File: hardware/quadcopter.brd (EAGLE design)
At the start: 126.2 x 126.2 mm, 85 parts, among them J1 AVR_SPI_PRG_6NS, J2 HEADER-4POS-0.1IN-FEMALE-SMD-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, J3 HEADER-10POSTH-254X10, J4 HEADER-4POS-0.1IN-FEMALE-SMD-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, M1 MOTOR_PADS_GND-MOLEX-SMD, M2 MOTOR_PADS_GND-MOLEX-SMD, M3 MOTOR_PADS_GND-MOLEX-SMD, M4 MOTOR_PADS_GND-MOLEX-SMD, Q1 MOSFET-SI2302CDS-T1-E3CT-ND, Q2 MOSFET-SI2302CDS-T1-E3CT-ND, Q3 MOSFET-SI2302CDS-T1-E3CT-ND, Q4 MOSFET-SI2302CDS-T1-E3CT-ND, Q5 MOSFET-SI2302CDS-T1-E3CT-ND, Q6 MOSFET-SI2302CDS-T1-E3CT-ND, Q7 MOSFET-SI2302CDS-T1-E3CT-ND, Q8 MOSFET-SI2302CDS-T1-E3CT-ND, Q9 MOSFET-SI2302CDS-T1-E3CT-ND, SW1 PUSHBUTTON_SMD-VERTICAL-1, U1 ATMEGA128RFA1, U2 LSM-IMU-497-18367-1-NDIMU, Y1 CRYSTAL5X3

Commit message: fixed quick check
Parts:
- moved R7 0.12 mm to (-3.00, -9.00)
- moved J4 0.05 mm to (-12.0, -14.0)
- renumbered NET_BRIDGE to NB, REG to RG
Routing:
- net VBAT: track 129.4 -> 93.1 mm, vias 19 -> 25
- net BAT_GND: track 85.3 -> 70.3 mm, vias 24 -> 26
- net GND: track 741.5 -> 737.6 mm
- net MISO: track 29.3 -> 30.3 mm
- net 3V: track 135.0 -> 134.0 mm
- net RED: track 395.8 -> 395.2 mm
- net BLU: track 234.4 -> 233.9 mm
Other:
- board text removed: "2 mm"
- board text removed: "height: 126.2 mm"

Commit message: fixed quickcheck part 2
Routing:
- net VBAT: track 93.1 -> 86.5 mm
- net GND: track 737.6 -> 741.4 mm
- net RED: track 395.2 -> 394.6 mm

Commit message: changed part names
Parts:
- renumbered NB to NB1, RG to RG1
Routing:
- net VBAT: vias 25 -> 24
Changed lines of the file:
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@@
 <attribute name="NAME" x="-17" y="24" size="0.9" layer="25" font="vector" align="center"/>
 </element>
-<element name="NB" library="custom_" library_urn="urn:adsk.wipprod:fs.file:vf.FjMADskDQ2Se9fX1PD5xcw" package="NET_BRIDGE" value="NET-BRIDGE" x="-2" y="-22.5" smashed="yes">
+<element name="NB1" library="custom_" library_urn="urn:adsk.wipprod:fs.file:vf.FjMADskDQ2Se9fX1PD5xcw" package="NET_BRIDGE" value="NET-BRIDGE" x="-2" y="-22.5" smashed="yes">
 <attribute name="CREATOR" value="ELAINE" x="27.21" y="-84.73" size="1.778" layer="27" display="off"/>
 <attribute name="DIST" value="NA" x="27.21" y="-84.73" size="1.778" layer="27" display="off"/>
@@
 <attribute name="VALUE" x="-22" y="6.5" size="0.9" layer="27" font="vector" align="center"/>
 </element>
-<element name="RG" library="quadparts_prebuilt_2022" package="SOT23-DBV" value="3V" x="-3" y="-16.5" smashed="yes">
+<element name="RG1" library="quadparts_prebuilt_2022" package="SOT23-DBV" value="3V" x="-3" y="-16.5" smashed="yes">
 <attribute name="CREATOR" value="Swanson" x="24.94" y="-46.98" size="1.778" layer="27" display="off"/>
 <attribute name="DATASHEET" value="http://www.ti.com/lit/ds/symlink/lp3985.pdf" x="24.94" y="-46.98" size="1.778" layer="27" display="off"/>
@@
 <contactref element="R22" pad="2"/>
 <contactref element="R21" pad="2"/>
-<contactref element="RG" pad="2"/>
+<contactref element="RG1" pad="2"/>
 <contactref element="C13" pad="2"/>
-<contactref element="NB" pad="2"/>
+<contactref element="NB1" pad="2"/>
 <contactref element="J4" pad="3"/>
 <contactref element="J3" pad="1"/>
@@
 <contactref element="R18" pad="1"/>
 <contactref element="R19" pad="1"/>
-<contactref element="RG" pad="5"/>
+<contactref element="RG1" pad="5"/>
 <contactref element="C13" pad="1"/>
 <contactref element="C17" pad="1"/>
@@
 <contactref element="D5" pad="1"/>
 <contactref element="S1" pad="B"/>
-<contactref element="RG" pad="1"/>
+<contactref element="RG1" pad="1"/>
 <contactref element="C15" pad="1"/>
 <contactref element="B2" pad="2"/>
@@
 <wire x1="30.870865625" y1="2.158478125" x2="30.5" y2="2.2346" width="0.762" layer="16"/>
 <wire x1="-3.95" y1="-17.8" x2="-3.9116" y2="-19.2637" width="0.762" layer="1"/>
-<via x="-4" y="-3.5" extent="1-16" drill="0.6096">
-</via>
 <via x="-18" y="5" extent="1-16" drill="0.6096">
 </via>
@@
 <contactref element="S1" pad="A"/>
 <contactref element="B2" pad="1"/>
-<contactref element="NB" pad="1"/>
+<contactref element="NB1" pad="1"/>
 <contactref element="J3" pad="4"/>
 <contactref element="R1" pad="1"/>
@@
 </signal>
 <signal name="N$20">
-<contactref element="RG" pad="3"/>
+<contactref element="RG1" pad="3"/>
 <contactref element="S1" pad="C"/>
 <wire x1="-1.1176" y1="-30.24505" x2="-2.30505" y2="-29.0576" width="0.127" layer="1"/>

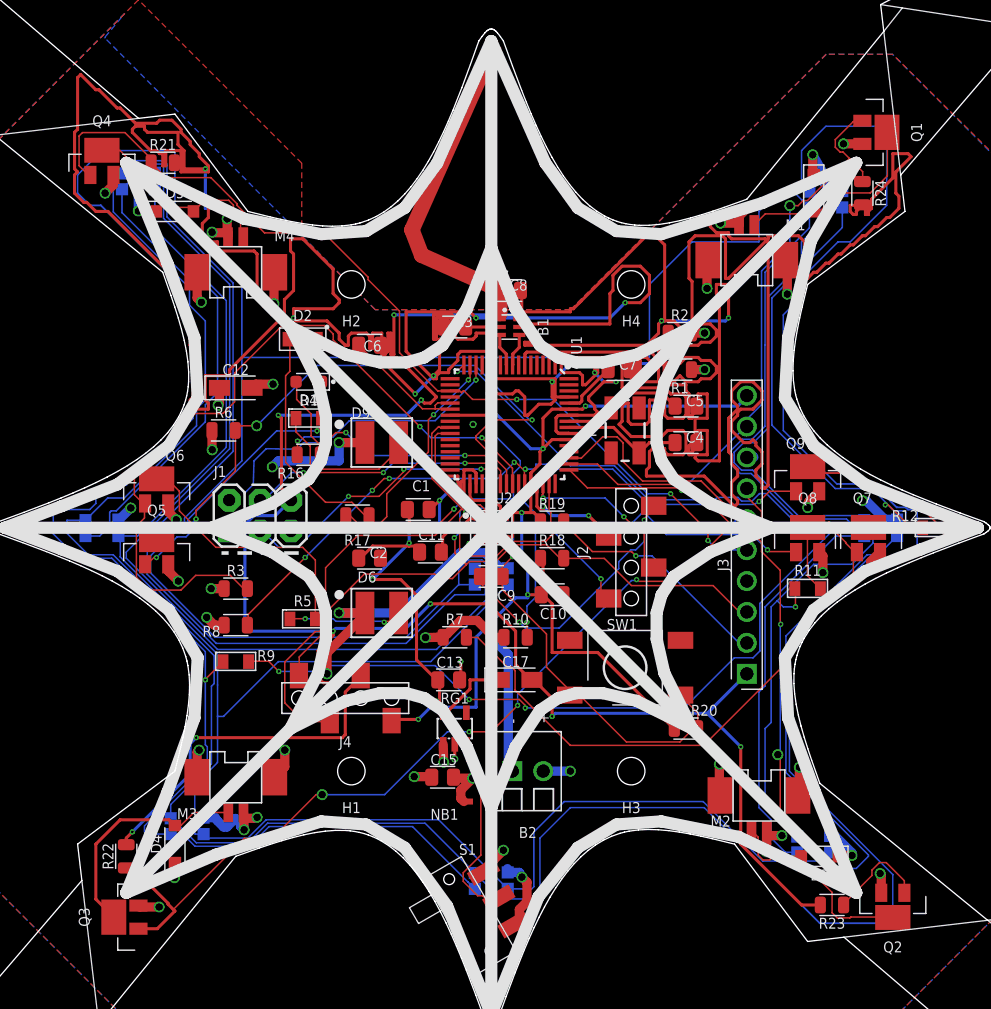
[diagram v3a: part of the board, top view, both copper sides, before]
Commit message: fixed full check issues
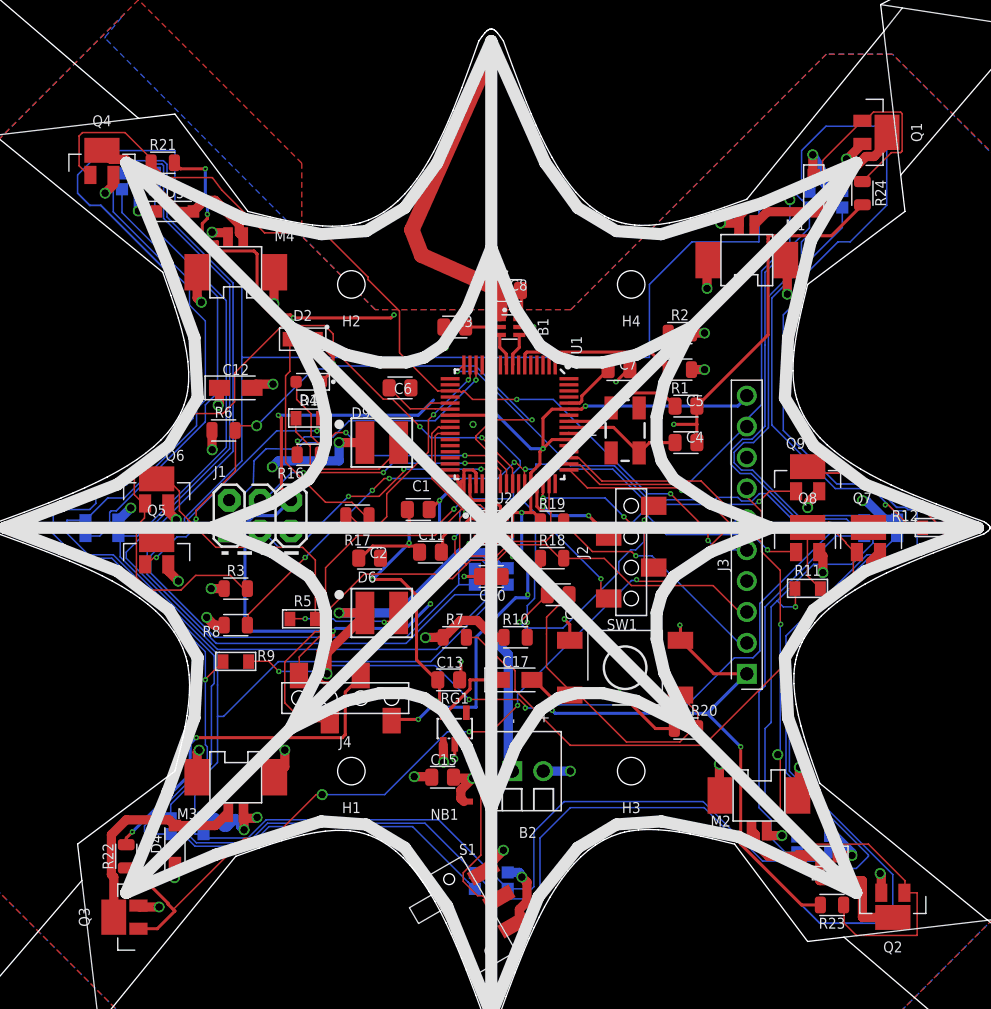
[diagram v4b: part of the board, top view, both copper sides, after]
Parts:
- moved C9 5.70 mm to (5.50, -5.50)
- moved C10 5.22 mm to (0.00, -4.00)
- moved C6 4.30 mm to (-7.50, 11.5)
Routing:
- net GND: track 741.4 -> 246.3 mm, vias 34 -> 31
- net 3V: track 134.0 -> 120.1 mm, vias 11 -> 14
- net PWM2: track 63.6 -> 72.4 mm
- net PWM1: track 51.1 -> 58.3 mm
- net VBAT: track 86.5 -> 83.0 mm, vias 24 -> 22
- net N$9: track 11.3 -> 8.05 mm
- net PWM3: track 89.2 -> 86.9 mm
- net RESET: track 66.7 -> 68.4 mm
- net N$11: track 22.1 -> 20.4 mm
- net N$14: track 16.2 -> 14.8 mm
- net N$16: track 19.0 -> 17.6 mm
- net BAT_GND: track 70.3 -> 69.1 mm
- net N$15: track 17.0 -> 17.9 mm
- net N$17: track 16.4 -> 15.7 mm

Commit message: finished fixing review
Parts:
- J1: value AVR_SPI_PRG_6NS -> AVR_SPI_PRG_6-SMD; device quadparts_prebuilt_2022:2X3-NS -> quadparts_prebuilt_2022:2X3-SMD
- moved R12 57.7 mm to (-21.0, -4.50), flipped to the bottom
- moved Q9 47.2 mm to (-21.0, -0.50), flipped to the bottom
- moved J1 47.2 mm to (28.2, -0.01), turned to 90 degrees
- moved R9 38.6 mm to (16.0, 0.00), flipped to the bottom
- moved Q8 34.7 mm to (0.00, -24.0), flipped to the bottom
- moved R11 27.6 mm to (6.00, -24.0), flipped to the bottom
- moved D1 26.6 mm to (-13.0, -14.5)
- moved R17 21.5 mm to (-32.5, 1.50)
- moved R16 19.0 mm to (-32.5, -1.50)
- moved R7 19.0 mm to (16.0, -10.0), flipped to the bottom
- moved R22 17.7 mm to (-17.0, -15.0)
- moved C9 17.6 mm to (-11.0, -11.5)
- moved R10 15.7 mm to (-5.00, -23.0), flipped to the bottom
- moved Q3 14.9 mm to (-20.0, -21.0)
- moved Q7 14.4 mm to (17.1, -4.50), flipped to the bottom
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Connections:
- net 3V: now also J1.2
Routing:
- net GND: track 246.3 -> 66.8 mm, vias 31 -> 25
- net SCK: track 23.3 -> 73.8 mm, vias 3 -> 8
- net MISO: track 30.3 -> 78.4 mm, vias 3 -> 10
- net N$1: track 6.86 -> 49.9 mm, vias 0 -> 4
- net PG2: track 86.4 -> 44.3 mm, vias 2 -> 7
- net PG0: track 19.1 -> 61.2 mm, vias 2 -> 5
- net RESET: track 68.4 -> 109.6 mm, vias 3 -> 7
- net N$2: track 19.0 -> 54.8 mm, vias 0 -> 4
- net PG1: track 19.5 -> 51.2 mm, vias 2 -> 6
- net MOSI: track 21.9 -> 47.1 mm, vias 3 -> 6
- net SCL: track 75.4 -> 51.6 mm
- net PB7: track 55.0 -> 34.4 mm, vias 6 -> 2
- net RED: track 394.6 -> 375.4 mm
- net PWM2: track 72.4 -> 53.9 mm
- net N$11: track 20.4 -> 37.8 mm, vias 2 -> 4
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
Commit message: fixed quick check
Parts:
- moved J1 0.19 mm to (28.0, 0.00)
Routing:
- net BAT_GND: track 62.9 -> 61.2 mm
- net 3V: track 123.8 -> 125.0 mm

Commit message: fixed quick check 2
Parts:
- moved Q7 0.07 mm to (17.0, -4.50)
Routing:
- net SCL: track 51.6 -> 52.5 mm
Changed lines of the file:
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@@
 <attribute name="VALUE" x="-29.5" y="-2.5" size="0.9" layer="28" font="vector" rot="MR0"/>
 </element>
-<element name="Q7" library="custom_" library_urn="urn:adsk.wipprod:fs.file:vf.FjMADskDQ2Se9fX1PD5xcw" package="SOT95P240X110-3MOSFET" value="MOSFET-SI2302CDS-T1-E3CT-ND" x="17.0726" y="-4.5" smashed="yes" rot="MR0">
-<attribute name="CREATOR" value="ELENA" x="23.0726" y="3.5" size="1.778" layer="28" rot="MR0" display="off"/>
-<attribute name="DIST" value="Digikey" x="23.0726" y="3.5" size="1.778" layer="28" rot="MR0" display="off"/>
-<attribute name="DISTPN" value="SI2302CDS-T1-E3CT-ND" x="23.0726" y="3.5" size="1.778" layer="28" rot="MR0" display="off"/>
-<attribute name="NAME" x="17.5726" y="-1.5" size="0.9" layer="26" font="vector" rot="MR0" align="bottom-center"/>
+<element name="Q7" library="custom_" library_urn="urn:adsk.wipprod:fs.file:vf.FjMADskDQ2Se9fX1PD5xcw" package="SOT95P240X110-3MOSFET" value="MOSFET-SI2302CDS-T1-E3CT-ND" x="17" y="-4.5" smashed="yes" rot="MR0">
+<attribute name="CREATOR" value="ELENA" x="23" y="3.5" size="1.778" layer="28" rot="MR0" display="off"/>
+<attribute name="DIST" value="Digikey" x="23" y="3.5" size="1.778" layer="28" rot="MR0" display="off"/>
+<attribute name="DISTPN" value="SI2302CDS-T1-E3CT-ND" x="23" y="3.5" size="1.778" layer="28" rot="MR0" display="off"/>
+<attribute name="NAME" x="17.5" y="-1.5" size="0.9" layer="26" font="vector" rot="MR0" align="bottom-center"/>
 </element>
 <element name="R7" library="quadparts_prebuilt_2022" package="RESC2012X60_HS" value="10K" x="16" y="-10" smashed="yes" rot="MR0">
@@
 <wire x1="21.5" y1="23.05" x2="20.26176875" y2="21.81176875" width="0.762" layer="1"/>
 <wire x1="20.26176875" y1="21.81176875" x2="20.18623125" y2="21.81176875" width="0.762" layer="1"/>
-<wire x1="16.955" y1="-10" x2="18.2546" y2="-10" width="0.762" layer="16"/>
 <wire x1="-20.045" y1="3.5" x2="-18.7454" y2="3.5" width="0.762" layer="16"/>
 <wire x1="-21.95" y1="-1.5" x2="-21.95" y2="-2.8596" width="0.762" layer="16"/>
-<via x="18.2546" y="-10" extent="1-16" drill="0.6096">
-</via>
 <via x="-18.7454" y="3.5" extent="1-16" drill="0.6096">
 </via>
@@
 <wire x1="-2.5" y1="-24" x2="-2.20434375" y2="-24" width="0.762" layer="16"/>
 <wire x1="-2.20434375" y1="-24" x2="-1.67094375" y2="-24.5334" width="0.762" layer="16"/>
-<via x="18" y="-7" extent="1-16" drill="0.762">
-</via>
-<wire x1="16.1226" y1="-5.5" x2="16.9892" y2="-6.3666" width="0.762" layer="16"/>
-<wire x1="16.9892" y1="-6.3666" x2="16.9892" y2="-6.47094375" width="0.762" layer="16"/>
-<wire x1="16.9892" y1="-6.47094375" x2="17.51825625" y2="-7" width="0.762" layer="16"/>
-<wire x1="17.51825625" y1="-7" x2="18" y2="-7" width="0.762" layer="16"/>
+<via x="17.75" y="-6.9739" extent="1-16" drill="0.762">
+</via>
 <via x="-17.67299375" y="-21.16489375" extent="1-16" drill="0.6096">
 </via>
@@
 <wire x1="-22.9166" y1="20.52905625" x2="-22.9166" y2="20.6334" width="0.762" layer="1"/>
 <wire x1="-22.9166" y1="20.6334" x2="-22.05" y2="21.5" width="0.762" layer="1"/>
+<via x="18.23839375" y="-10.01620625" extent="1-16" drill="0.6096">
+</via>
+<wire x1="16.955" y1="-10" x2="18.2221875" y2="-10" width="0.762" layer="16"/>
+<wire x1="18.2221875" y1="-10" x2="18.23839375" y2="-10.01620625" width="0.762" layer="16"/>
+<wire x1="16.05" y1="-5.5" x2="16.9166" y2="-6.3666" width="0.762" layer="16"/>
+<wire x1="16.9166" y1="-6.3666" x2="16.9166" y2="-6.47094375" width="0.762" layer="16"/>
+<wire x1="16.9166" y1="-6.47094375" x2="17.41955625" y2="-6.9739" width="0.762" layer="16"/>
+<wire x1="17.41955625" y1="-6.9739" x2="17.75" y2="-6.9739" width="0.762" layer="16"/>
 </signal>
 <signal name="PWM2">
@@
 <wire x1="10.5444125" y1="-13.0444125" x2="8.990175" y2="-14.59865" width="0.127" layer="16"/>
 <wire x1="8.990175" y1="-14.59865" x2="2.16535" y2="-14.59865" width="0.127" layer="16"/>
-<wire x1="16.028825" y1="-7.56" x2="12.729675" y2="-4.26085" width="0.127" layer="16"/>
-<wire x1="11.94435" y1="-4.26085" x2="12.729675" y2="-4.26085" width="0.127" layer="16"/>
-<wire x1="16.028825" y1="-7.56" x2="16.028825" y2="-8.971175" width="0.127" layer="16"/>
 <wire x1="16.028825" y1="-8.971175" x2="16" y2="-9" width="0.127" layer="16"/>
 <wire x1="16" y1="-9" x2="15.9555875" y2="-9.0444125" width="0.127" layer="16"/>
@@
 <wire x1="14.5" y1="-13" x2="14.4555875" y2="-13.0444125" width="0.127" layer="16"/>
 <wire x1="14.4555875" y1="-13.0444125" x2="10.5444125" y2="-13.0444125" width="0.127" layer="16"/>
+<wire x1="11.94435" y1="-4.26085" x2="13.6273" y2="-5.9438" width="0.127" layer="16"/>
+<wire x1="13.6273" y1="-5.9438" x2="13.6273" y2="-6.45516875" width="0.127" layer="16"/>
+<wire x1="16.028825" y1="-8.85669375" x2="16.028825" y2="-8.971175" width="0.127" layer="16"/>
+<wire x1="13.6273" y1="-6.45516875" x2="16.028825" y2="-8.85669375" width="0.127" layer="16"/>
 </signal>
 <signal name="PWM4">
@@
 <wire x1="-2.0955" y1="1.2573" x2="-2.4445" y2="0.9083" width="0.127" layer="1"/>
 <wire x1="-2.4445" y1="0.9083" x2="-2.4445" y2="-1.31291875" width="0.127" layer="1"/>
-<wire x1="11.8745" y1="-2.30505" x2="15.4067" y2="-5.83725" width="0.127" layer="16"/>
-<wire x1="15.4067" y1="-5.83725" x2="15.4067" y2="-6.33943125" width="0.127" layer="16"/>
-<wire x1="19.10385625" y1="-9.42975" x2="20.955" y2="-9.42975" width="0.127" layer="16"/>
+<wire x1="11.8745" y1="-2.30505" x2="13.9067" y2="-4.33725" width="0.127" layer="16"/>
+<wire x1="13.9067" y1="-4.33725" x2="13.9067" y2="-6.33943125" width="0.127" layer="16"/>
+<wire x1="18.60385625" y1="-9.42975" x2="20.955" y2="-9.42975" width="0.127" layer="16"/>
 <wire x1="-3.3491" y1="-1.65391875" x2="-2.73" y2="-2.27301875" width="0.127" layer="1"/>
 <wire x1="-2.73" y1="-2.27301875" x2="-2.73" y2="-4.65" width="0.127" layer="1"/>
@@
 <wire x1="-4.67995" y1="7.9629" x2="-4.67995" y2="3.84175" width="0.127" layer="1"/>
 <wire x1="-4.67995" y1="3.84175" x2="-2.409825" y2="1.571625" width="0.127" layer="1"/>
-<wire x1="15.4067" y1="-6.33943125" x2="16.23436875" y2="-7.1671" width="0.127" layer="16"/>
-<wire x1="16.23436875" y1="-7.1671" x2="16.84120625" y2="-7.1671" width="0.127" layer="16"/>
-<wire x1="16.84120625" y1="-7.1671" x2="19.10385625" y2="-9.42975" width="0.127" layer="16"/>
+<wire x1="13.9067" y1="-6.33943125" x2="14.73436875" y2="-7.1671" width="0.127" layer="16"/>
+<wire x1="14.73436875" y1="-7.1671" x2="16.34120625" y2="-7.1671" width="0.127" layer="16"/>
+<wire x1="16.34120625" y1="-7.1671" x2="18.60385625" y2="-9.42975" width="0.127" layer="16"/>
 </signal>
 <signal name="SDA">
@@
 <wire x1="-17.493" y1="-11.80465" x2="-14.2565625" y2="-11.80465" width="0.127" layer="16"/>
 <wire x1="14.95" y1="0" x2="17.0726" y2="-2.1226" width="0.127" layer="16"/>
-<wire x1="17.0726" y1="-2.1226" x2="17.0726" y2="-3.475" width="0.127" layer="16"/>
+<wire x1="17.0726" y1="-2.1226" x2="17" y2="-3.475" width="0.127" layer="16"/>
 <wire x1="17.25" y1="-3.5" x2="20.25" y2="-3.5" width="0.127" layer="16"/>
 <wire x1="20.25" y1="-3.5" x2="20.75" y2="-3" width="0.127" layer="16"/>
-<wire x1="17.0726" y1="-3.475" x2="17.25" y2="-3.5" width="0.127" layer="16"/>
+<wire x1="17" y1="-3.475" x2="17.25" y2="-3.5" width="0.127" layer="16"/>
 <via x="2.794" y="-15.32255" extent="1-16" drill="0.2032">
 </via>
@@
 <via x="18.5" y="-8" extent="1-16" drill="0.2032">
 </via>
-<via x="17.5" y="-8.5" extent="1-16" drill="0.2032">
-</via>
-<wire x1="19" y1="-6.4774" x2="18.0226" y2="-5.5" width="0.127" layer="16"/>
+<wire x1="19" y1="-6.4774" x2="17.95" y2="-5.5" width="0.127" layer="16"/>
 <wire x1="19" y1="-8" x2="19" y2="-6.4774" width="0.127" layer="16"/>
 <wire x1="19" y1="-8" x2="18.5" y2="-8" width="0.127" layer="16"/>
-<wire x1="17.5" y1="-8.5" x2="16.9059" y2="-9.0941" width="0.127" layer="16"/>
-<wire x1="16.9059" y1="-9.0941" x2="16.5403" y2="-9.0941" width="0.127" layer="16"/>
-<wire x1="15.6344" y1="-10" x2="15.045" y2="-10" width="0.127" layer="16"/>
-<wire x1="16.5403" y1="-9.0941" x2="15.6344" y2="-10" width="0.127" layer="16"/>
+<wire x1="16.5403" y1="-9.0941" x2="16.9059" y2="-9.0941" width="0.127" layer="16"/>
+<wire x1="15.045" y1="-10" x2="15.6344" y2="-10" width="0.127" layer="16"/>
+<wire x1="15.6344" y1="-10" x2="16.5403" y2="-9.0941" width="0.127" layer="16"/>
 <wire x1="18.5" y1="-8" x2="18" y2="-8.5" width="0.127" layer="1"/>
 <wire x1="18" y1="-8.5" x2="17.5" y2="-8.5" width="0.127" layer="1"/>
@@
 <wire x1="16.75" y1="2.5" x2="16.75" y2="1.5" width="0.127" layer="1"/>
 <wire x1="16.75" y1="2.30505" x2="16.75" y2="2.5" width="0.127" layer="16"/>
-<wire x1="18.25" y1="-5.5" x2="18.0226" y2="-5.5" width="0.127" layer="16"/>
+<wire x1="18.25" y1="-5.5" x2="17.95" y2="-5.5" width="0.127" layer="16"/>
 <via x="19.75" y="-4" extent="1-16" drill="0.2032">
 </via>
@@
 <via x="16.75" y="2.5" extent="1-16" drill="0.2032">
 </via>
+<via x="17.2727375" y="-8.7272625" extent="1-16" drill="0.2032">
+</via>
+<wire x1="17.5" y1="-8.5" x2="17.2727375" y2="-8.7272625" width="0.127" layer="1"/>
+<wire x1="16.9059" y1="-9.0941" x2="17.2727375" y2="-8.7272625" width="0.127" layer="16"/>
 </signal>
 <signal name="PB6">
